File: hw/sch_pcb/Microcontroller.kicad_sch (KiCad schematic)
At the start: 28 parts, among them J1 HEADER_2x01_PARALLEL, J2 HEADER_2x01, J3 HEADER_2x03, U1 ISL21080CIH320Z-TK, U2 LM4041CIM3-1.2(neosazovat), U3 ATMEGA1284P-AU, Y6 8MHz LFXTAL083138

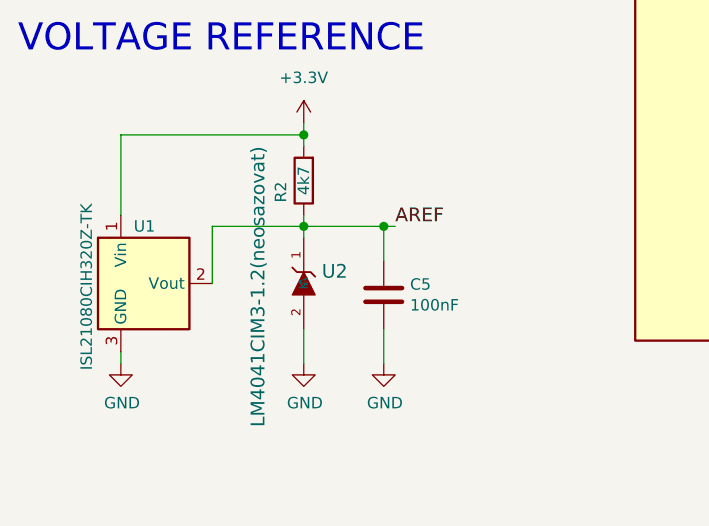
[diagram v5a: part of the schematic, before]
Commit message: Update footprints. Improve layout Fix some DRC errors. Set components values matching inventory.
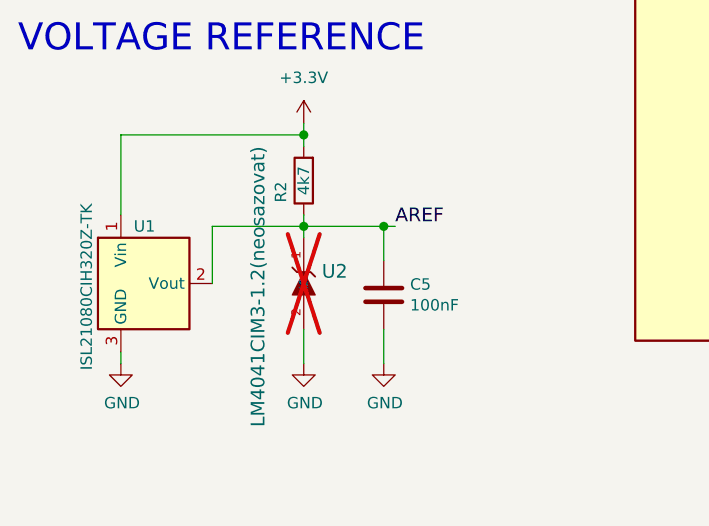
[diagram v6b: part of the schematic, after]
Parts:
- C1, C10, C2, C3, C4, C5, C6, C7, C8, C9: footprint Mlab_C:SMD-0805 -> Capacitor_SMD:C_0805_2012Metric
- R1, R10, R11, R2, R3, R48, R5, R6, R8, R9: footprint Mlab_R:SMD-0805 -> Resistor_SMD:R_0805_2012Metric
- U2: now not fitted
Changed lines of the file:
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@@
 			)
 		)
-		(property "Footprint" "Mlab_C:SMD-0805"
+		(property "Footprint" "Capacitor_SMD:C_0805_2012Metric"
 			(at 71.12 77.1652 0)
 			(effects
@@
 			)
 		)
-		(property "Footprint" "Mlab_C:SMD-0805"
+		(property "Footprint" "Capacitor_SMD:C_0805_2012Metric"
 			(at 63.1952 165.1 0)
 			(effects
@@
 			)
 		)
-		(property "Footprint" "Mlab_R:SMD-0805"
+		(property "Footprint" "Resistor_SMD:R_0805_2012Metric"
 			(at 158.242 93.98 90)
 			(effects
@@
 			)
 		)
-		(property "Footprint" "Mlab_R:SMD-0805"
+		(property "Footprint" "Resistor_SMD:R_0805_2012Metric"
 			(at 249.682 36.83 90)
 			(effects
@@
 			)
 		)
-		(property "Footprint" "Mlab_C:SMD-0805"
+		(property "Footprint" "Capacitor_SMD:C_0805_2012Metric"
 			(at 46.6852 34.29 0)
 			(effects
@@
 			)
 		)
-		(property "Footprint" "Mlab_C:SMD-0805"
+		(property "Footprint" "Capacitor_SMD:C_0805_2012Metric"
 			(at 80.9752 116.84 0)
 			(effects
@@
 			)
 		)
-		(property "Footprint" "Mlab_R:SMD-0805"
+		(property "Footprint" "Resistor_SMD:R_0805_2012Metric"
 			(at 163.322 93.98 90)
 			(effects
@@
 			)
 		)
-		(property "Footprint" "Mlab_C:SMD-0805"
+		(property "Footprint" "Capacitor_SMD:C_0805_2012Metric"
 			(at 66.04 85.3948 0)
 			(effects
@@
 			)
 		)
-		(property "Footprint" "Mlab_R:SMD-0805"
+		(property "Footprint" "Resistor_SMD:R_0805_2012Metric"
 			(at 173.482 93.98 90)
 			(effects
@@
 			)
 		)
-		(property "Footprint" "Mlab_R:SMD-0805"
+		(property "Footprint" "Resistor_SMD:R_0805_2012Metric"
 			(at 55.118 148.59 90)
 			(effects
@@
 			)
 		)
-		(property "Footprint" "Mlab_R:SMD-0805"
+		(property "Footprint" "Resistor_SMD:R_0805_2012Metric"
 			(at 168.402 93.98 90)
 			(effects
@@
 			)
 		)
-		(property "Footprint" "Mlab_C:SMD-0805"
+		(property "Footprint" "Capacitor_SMD:C_0805_2012Metric"
 			(at 45.72 95.5548 0)
 			(effects
@@
 			)
 		)
-		(property "Footprint" "Mlab_R:SMD-0805"
+		(property "Footprint" "Resistor_SMD:R_0805_2012Metric"
 			(at 50.038 82.55 90)
 			(effects
@@
 		(in_bom yes)
 		(on_board yes)
-		(dnp no)
+		(dnp yes)
 		(property "Reference" "U2"
 			(at 55.3466 158.6738 90)
@@
 			)
 		)
+		(property "UST_ID" ""
+			(at 53.34 160.02 0)
+			(effects
+				(font
+					(size 1.27 1.27)
+				)
+				(hide yes)
+			)
+		)
 		(pin "1"
 		)
@@
 			)
 		)
-		(property "Footprint" "Mlab_R:SMD-0805"
+		(property "Footprint" "Resistor_SMD:R_0805_2012Metric"
 			(at 84.328 68.58 90)
 			(effects
@@
 			)
 		)
-		(property "Footprint" "Mlab_R:SMD-0805"
+		(property "Footprint" "Resistor_SMD:R_0805_2012Metric"
 			(at 236.982 36.83 90)
 			(effects
@@
 			)
 		)
-		(property "Footprint" "Mlab_C:SMD-0805"
+		(property "Footprint" "Capacitor_SMD:C_0805_2012Metric"
 			(at 91.1352 34.29 0)
 			(effects
@@
 			)
 		)
-		(property "Footprint" "Mlab_C:SMD-0805"
+		(property "Footprint" "Capacitor_SMD:C_0805_2012Metric"
 			(at 69.5452 116.84 0)
 			(effects
@@
 			)
 		)
-		(property "Footprint" "Mlab_R:SMD-0805"
+		(property "Footprint" "Resistor_SMD:R_0805_2012Metric"
 			(at 153.162 74.93 90)
 			(effects
@@
 			)
 		)
-		(property "Footprint" "Mlab_C:SMD-0805"
+		(property "Footprint" "Capacitor_SMD:C_0805_2012Metric"
 			(at 58.1152 34.29 0)
 			(effects
@@
 			)
 		)
-		(property "Footprint" "Mlab_C:SMD-0805"
+		(property "Footprint" "Capacitor_SMD:C_0805_2012Metric"
 			(at 69.5452 34.29 0)
 			(effects
